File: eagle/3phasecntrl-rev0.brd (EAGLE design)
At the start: 92 x 88.5 mm, 66 parts, among them IC3 ATXmega32A4U, IC4 LD1117S50, IC6 LD1117S33, T1 BC847, T2 BC847, U1 LM5008MM

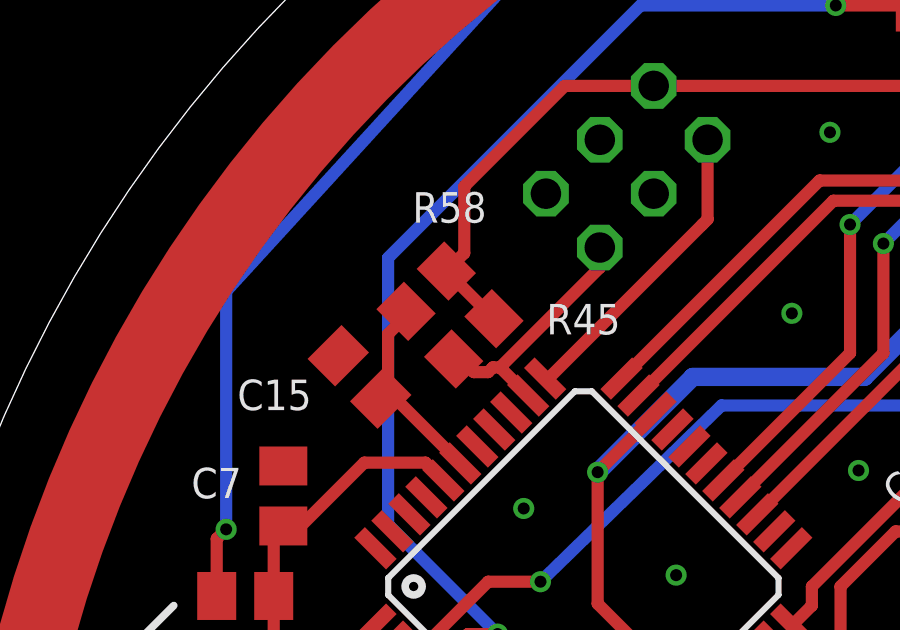
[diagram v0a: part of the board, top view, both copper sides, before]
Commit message: Added farnell parts to eagledb file, BOM.
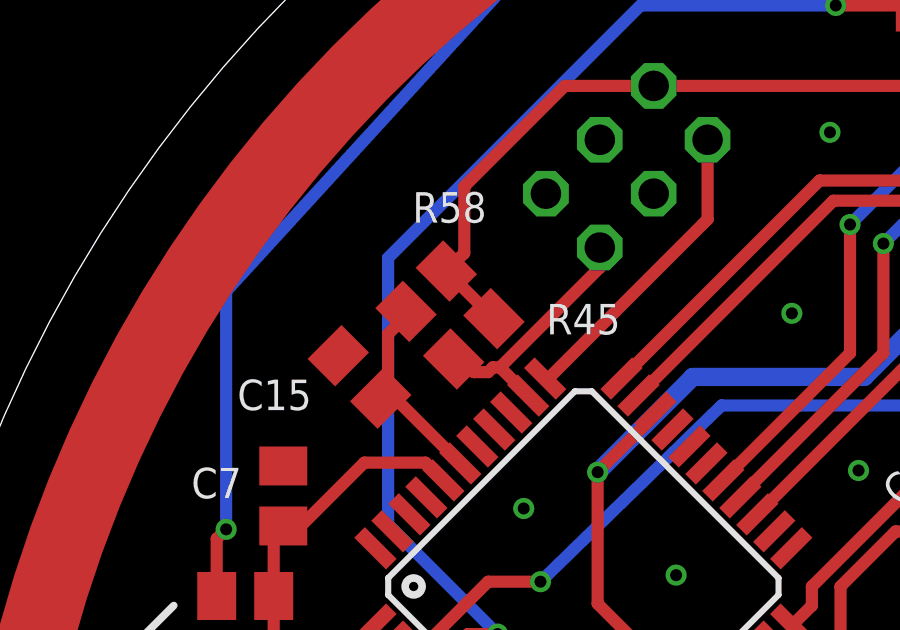
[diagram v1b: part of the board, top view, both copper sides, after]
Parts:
- C2: value 100 -> 100n
- C5: value 33u/25V -> 68u/25V
- C7: value 100n? -> 100n
- D1: value BAT46WH -> SS110B
- F1: value (none) -> 140mA
- R12: value 1k? -> 1k
- R29: value 220k -> 240k
- R45, R58: device rcl:R0805 -> rcl:M0805
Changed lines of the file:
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@@
 <attribute name="VALUE" x="-17.15" y="-9.89" size="1.016" layer="27" rot="R90"/>
 </element>
-<element name="D1" library="diode" package="SMB" value="BAT46WH" x="25.0825" y="-15.39875" smashed="yes" rot="R270">
+<element name="D1" library="diode" package="SMB" value="SS110B" x="25.0825" y="-15.39875" smashed="yes" rot="R270">
 <attribute name="NAME" x="27.84475" y="-21.0185" size="1.27" layer="25"/>
 <attribute name="VALUE" x="21.6535" y="-13.23975" size="1.27" layer="27" rot="R270"/>
@@
 <attribute name="VALUE" x="-19.812296875" y="3.36611875" size="1.778" layer="27" rot="R45"/>
 </element>
-<element name="R45" library="rcl" package="R0805" value="1k" x="-26.51125" y="20.955" smashed="yes" rot="R45">
+<element name="R45" library="rcl" package="M0805" value="1k" x="-26.51125" y="20.955" smashed="yes" rot="R45">
 <attribute name="NAME" x="-24.091478125" y="21.102465625" size="1.016" layer="25"/>
 <attribute name="VALUE" x="-25.164209375" y="18.709934375" size="1.27" layer="27" rot="R45"/>
@@
 <attribute name="VALUE" x="-9.841103125" y="13.1893875" size="1.016" layer="27" rot="R45"/>
 </element>
-<element name="R58" library="rcl" package="R0805" value="2R2" x="-28.09875" y="22.5425" smashed="yes" rot="R45">
+<element name="R58" library="rcl" package="M0805" value="2R2" x="-28.09875" y="22.5425" smashed="yes" rot="R45">
 <attribute name="NAME" x="-28.5557375" y="24.82745" size="1.016" layer="25"/>
 <attribute name="VALUE" x="-26.751709375" y="20.297434375" size="1.27" layer="27" rot="R45"/>
@@
 <attribute name="VALUE" x="18.24188125" y="23.856359375" size="1.27" layer="27" ratio="10" rot="R315"/>
 </element>
-<element name="F1" library="adafruit" package="1812" value="" x="30.1625" y="-15.4875" smashed="yes" rot="R270">
+<element name="F1" library="adafruit" package="1812" value="140mA" x="30.1625" y="-15.4875" smashed="yes" rot="R270">
 <attribute name="VALUE" x="32.0675" y="-13.63" size="0.6096" layer="27" rot="R270"/>
 <attribute name="NAME" x="32.83875" y="-16.03375" size="1.016" layer="25"/>
@@
 <attribute name="VALUE" x="35.2425" y="-3.65125" size="1.27" layer="27" rot="R180"/>
 </element>
-<element name="R29" library="rcl" package="M0805" value="220k" x="24.92375" y="-8.5725" smashed="yes" rot="R270">
+<element name="R29" library="rcl" package="M0805" value="240k" x="24.92375" y="-8.5725" smashed="yes" rot="R270">
 <attribute name="NAME" x="26.82875" y="-11.7475" size="1.016" layer="25"/>
 <attribute name="VALUE" x="22.38375" y="-7.3025" size="1.27" layer="27" rot="R270"/>
 </element>
-<element name="C5" library="rcl" package="153CLV-0605" value="33u/25V" x="20.0025" y="6.22875" smashed="yes" rot="R90">
+<element name="C5" library="rcl" package="153CLV-0605" value="68u/25V" x="20.0025" y="6.22875" smashed="yes" rot="R90">
 <attribute name="NAME" x="14.11" y="8.71" size="1.016" layer="25"/>
 <attribute name="VALUE" x="24.8875" y="2.80375" size="1.27" layer="27" rot="R90"/>
@@
 <attribute name="VALUE" x="-7.37" y="31.77" size="1.27" layer="27"/>
 </element>
-<element name="C2" library="rcl" package="C0805K" value="100" x="-30.851971875" y="7.248025" smashed="yes" rot="R225">
+<element name="C2" library="rcl" package="C0805K" value="100n" x="-30.851971875" y="7.248025" smashed="yes" rot="R225">
 <attribute name="NAME" x="-34.4736875" y="4.514971875" size="1.016" layer="25"/>
 <attribute name="VALUE" x="-31.488365625" y="9.298634375" size="1.016" layer="27" rot="R225"/>
@@
 <attribute name="VALUE" x="-30.9693875" y="-15.873603125" size="1.016" layer="27" rot="R135"/>
 </element>
-<element name="R12" library="rcl" package="M0805" value="1k?" x="-10.845" y="31.9975" smashed="yes">
+<element name="R12" library="rcl" package="M0805" value="1k" x="-10.845" y="31.9975" smashed="yes">
 <attribute name="NAME" x="-12.115" y="33.2675" size="1.016" layer="25"/>
 <attribute name="VALUE" x="-12.115" y="29.4575" size="1.27" layer="27"/>
@@
 <attribute name="VALUE" x="-35.40125" y="7.3025" size="1.27" layer="27"/>
 </element>
-<element name="C7" library="rcl" package="C0805K" value="100n?" x="-32.86125" y="15.71625" smashed="yes" rot="R90">
+<element name="C7" library="rcl" package="C0805K" value="100n" x="-32.86125" y="15.71625" smashed="yes" rot="R90">
 <attribute name="NAME" x="-35.925" y="15.63875" size="1.016" layer="25"/>
 <attribute name="VALUE" x="-30.96125" y="14.71625" size="1.016" layer="27" rot="R90"/>
